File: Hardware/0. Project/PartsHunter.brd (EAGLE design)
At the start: 214 x 147 mm, 54 parts, among them IC1 PCF8574P, IC2 LM1117-3.3, Q1 16 MHz, U1 ATMEGA328P-AU

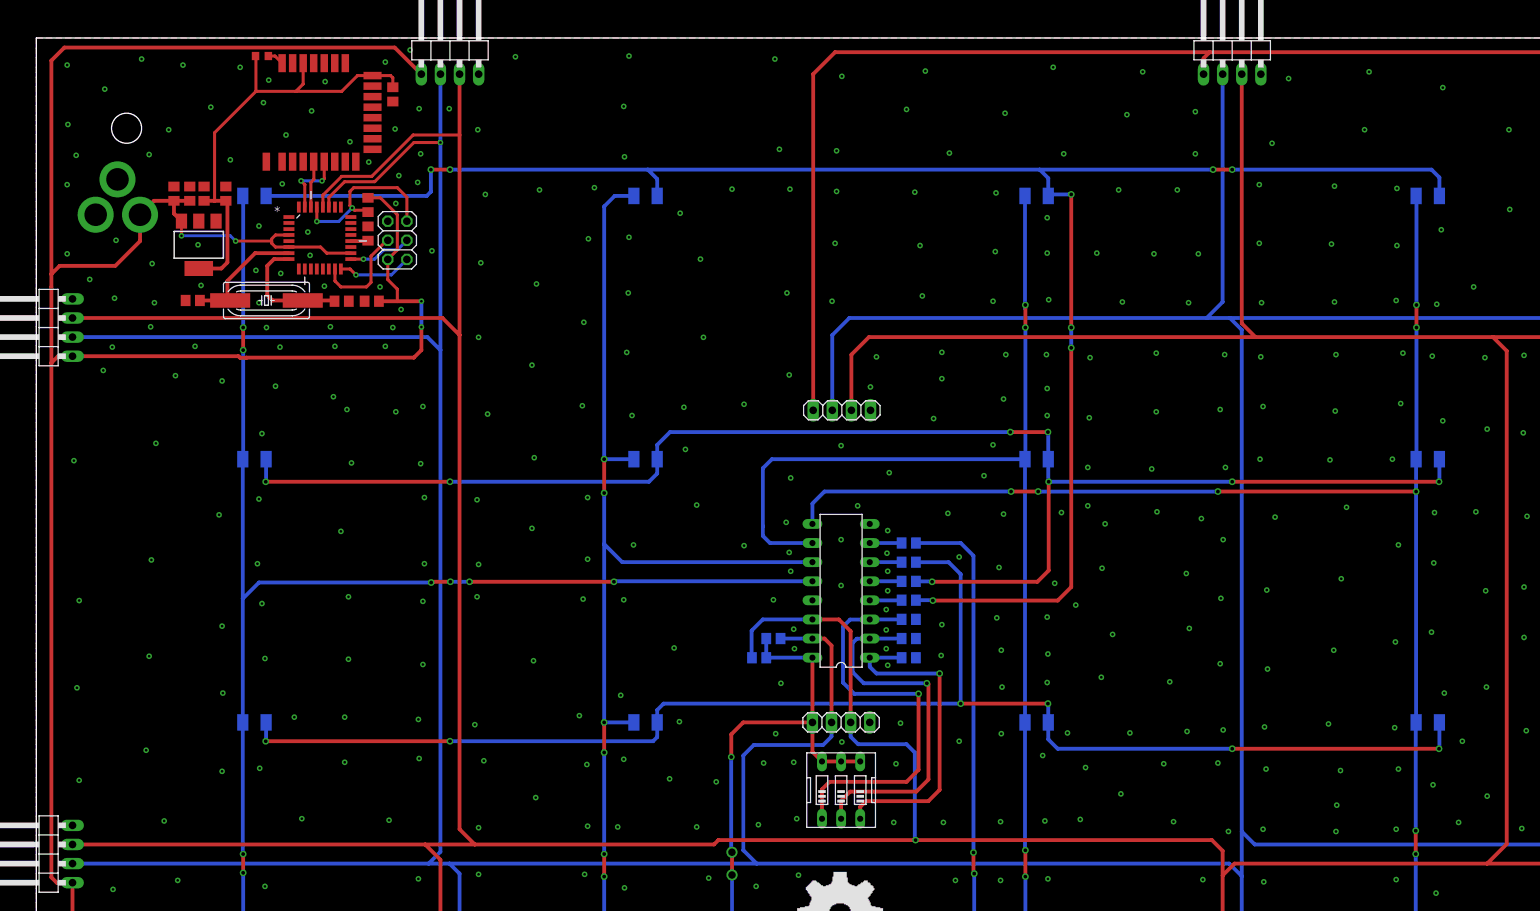
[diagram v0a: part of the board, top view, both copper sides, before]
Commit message: I2C pull-ups moved to master's circuit area
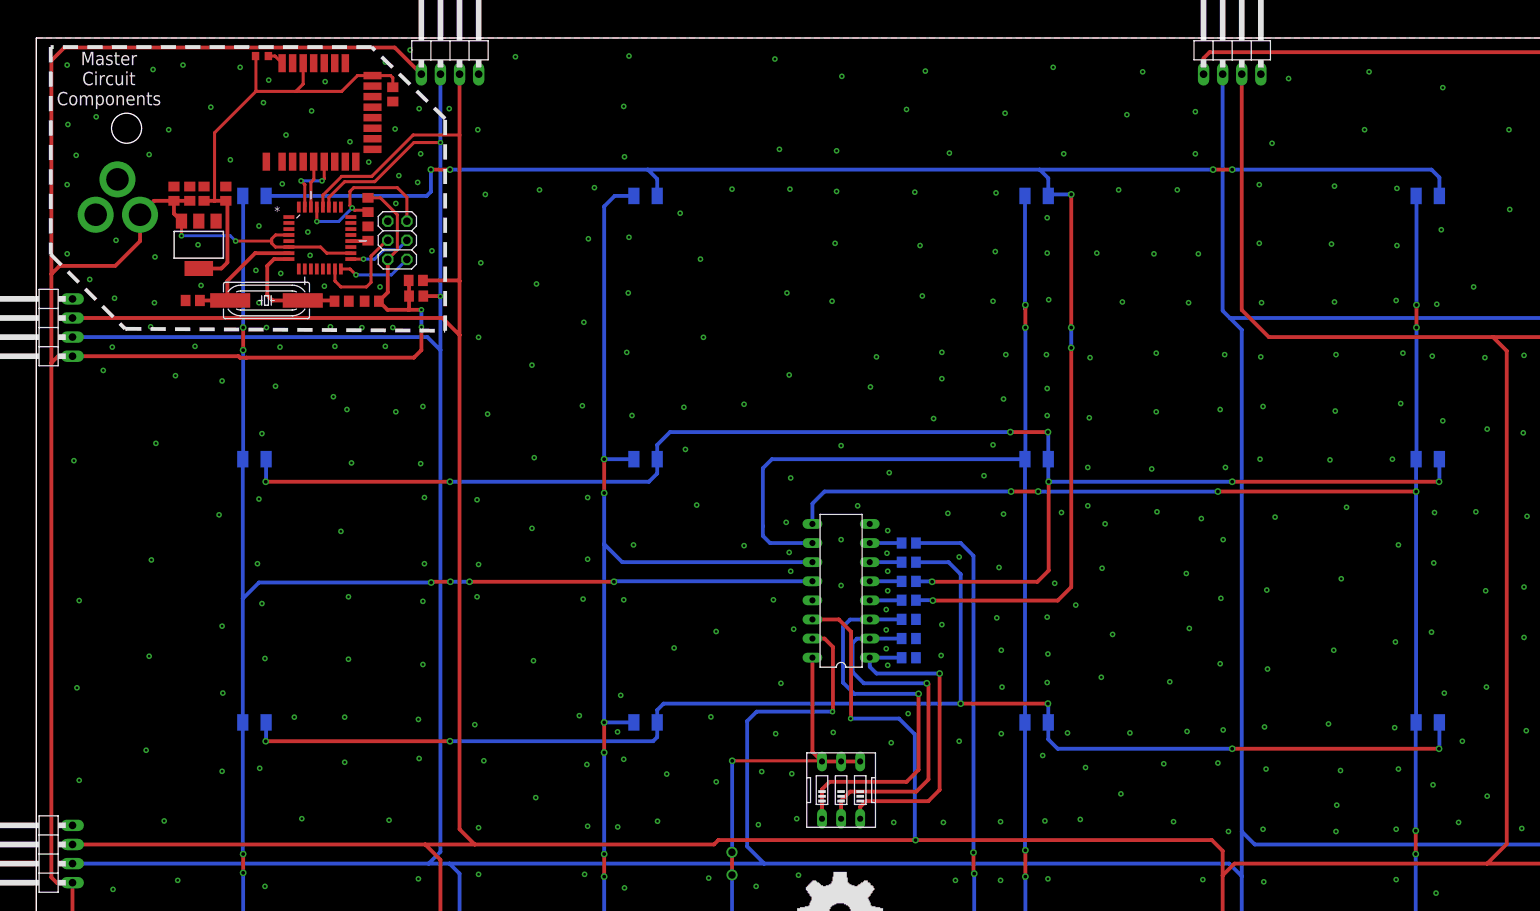
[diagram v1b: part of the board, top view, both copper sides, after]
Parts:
- removed JP10: (no value), pinhead:1X04
- removed JP12: ICSP, pinhead:2X03
- C3, C4: value 100 nF -> 22pF
- C6: value 10 uF -> 100 nF
- C7: value 22pF -> 10 uF
- C8: value 22pF -> 100 nF
- JP5: device pinhead:1X04 -> pinhead:1X04/90
- JP9: value (none) -> ICSP; device pinhead:1X04/90 -> pinhead:2X03
- R11: device rcl:R0603 -> rcl:R0805
- R6, R7: value 10k -> 72R
- R8: value 72R -> 10k; device rcl:R0805 -> rcl:R0603
- R9: value 72R -> 10k
- moved JP7 212.0 mm to (213.0, 38.5), turned to 270 degrees
- moved JP6 120.3 mm to (1.00, 38.5), turned to 90 degrees
- moved JP8 120.3 mm to (159.0, 146.0), turned to 0 degrees
- moved R11 117.5 mm to (116.0, 64.6), flipped to the bottom, turned to 180 degrees
- moved JP9 114.0 mm to (48.0, 120.1), turned to 90 degrees
- moved R8 109.2 mm to (30.0, 144.6), flipped to the top
- moved JP5 103.9 mm to (55.0, 146.0)
- moved R10 92.2 mm to (116.0, 67.2), flipped to the bottom, turned to 180 degrees
- moved R3 79.5 mm to (44.1, 124.8), flipped to the top, turned to 270 degrees
- moved R5 78.3 mm to (50.5, 112.7), flipped to the top, turned to 0 degrees
- moved R4 67.3 mm to (50.5, 114.8), flipped to the top, turned to 0 degrees
- moved C3 38.2 mm to (20.8, 112.1), turned to 0 degrees
- moved C5 25.8 mm to (47.4, 139.5), turned to 270 degrees
- moved C4 24.7 mm to (40.6, 112.0), turned to 180 degrees
- moved C8 24.7 mm to (20.4, 126.3), turned to 90 degrees
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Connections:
- net +5V: now also C8.1, C9.1, JP9.2, R5.1; no longer C4.1, C6.1, JP10.1, JP12.2, JP9.1, R10.1
- net 0V: now also C3.1, C4.1, C7.2, C8.2, JP9.6, R10.2, R11.2, R9.2; no longer C3.2, C4.2, C7.1, C8.1, JP10.4, JP12.6, JP9.4, R5.2, R6.2, R7.2
- net 3.3V: now also C6.1, C7.1, R8.1; no longer C3.1, C9.1, R11.1
- net BLE_WAKE: now also R8.2; no longer R11.2
- net ICSP_MISO: now also JP9.1; no longer JP12.1
- net ICSP_MOSI: now also JP9.4; no longer JP12.4
- net ICSP_RESET: now also JP9.5, R3.2; no longer JP12.5, R10.2
- net ICSP_SCK: now also JP9.3; no longer JP12.3
- net N$1: now also C3.2; no longer C7.2
- net N$2: now also C4.2; no longer C8.2
- net N$7: now also R6.1; no longer R8.1
- net N$8: now also R7.1; no longer R9.1
- net ROW_3: now also R6.2; no longer R8.2
- net ROW_4: now also R7.2; no longer R9.2
- net SCL: now also R4.2; no longer JP10.3, JP9.3, R3.2
- net SDA: now also R5.2; no longer JP10.2, JP9.2, R4.2
- net SLAVE_ADDR_A0: now also R11.1; no longer R7.1
- net SLAVE_ADDR_A1: now also R10.1; no longer R6.1
- net SLAVE_ADDR_A2: now also R9.1; no longer R5.1
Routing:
- net +5V: track 935.8 -> 828.6 mm
- net SCL: track 724.5 -> 654.0 mm, vias 1 -> 2
- net SDA: track 713.5 -> 648.0 mm, vias 1 -> 3
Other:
- board text added: "Master Circuit Components"

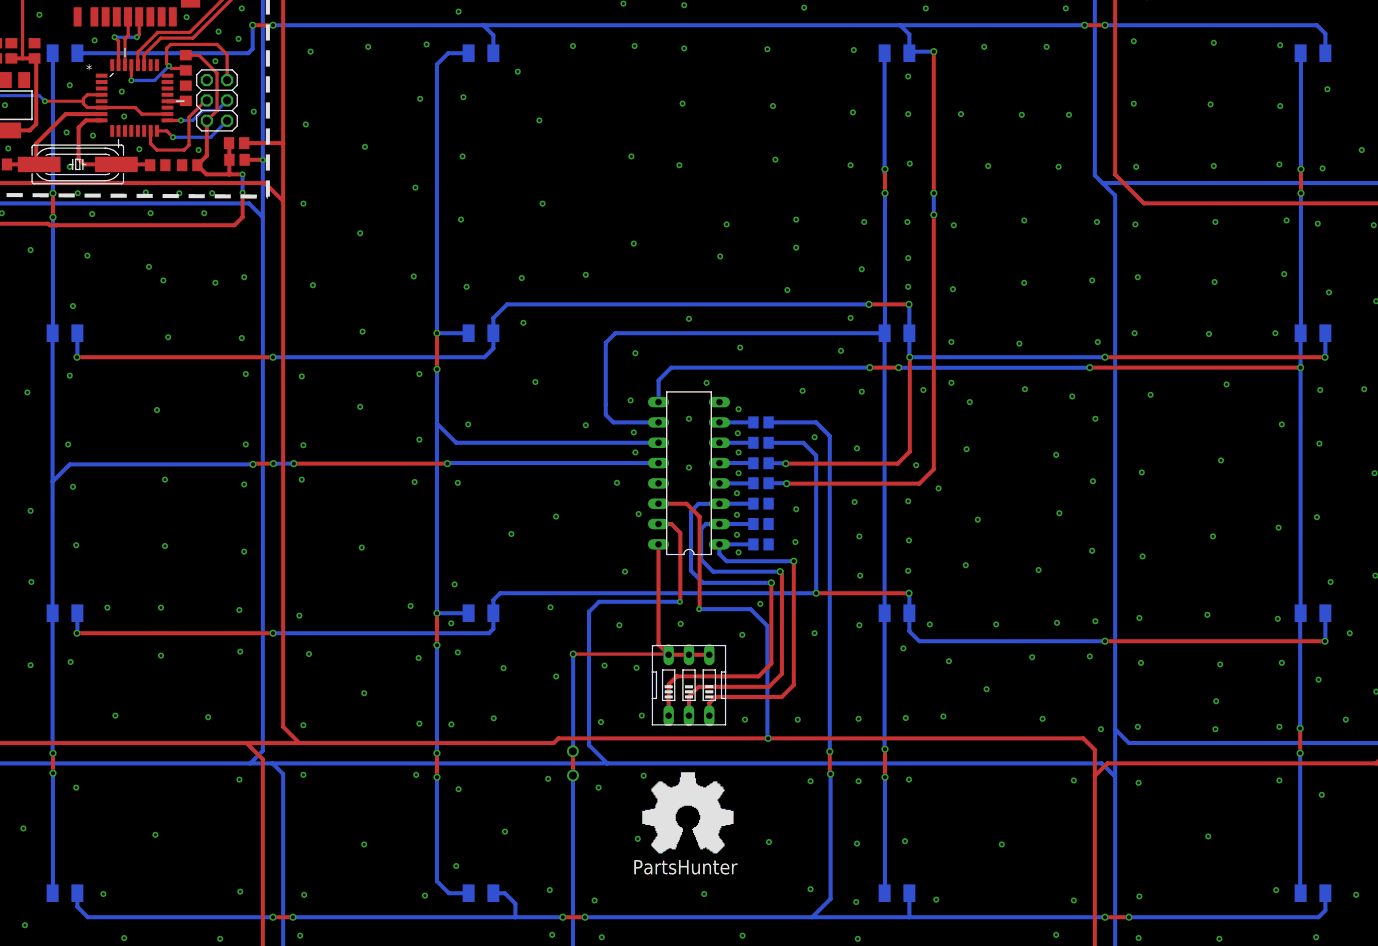
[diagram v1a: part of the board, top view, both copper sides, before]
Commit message: SMD and PTH led option added
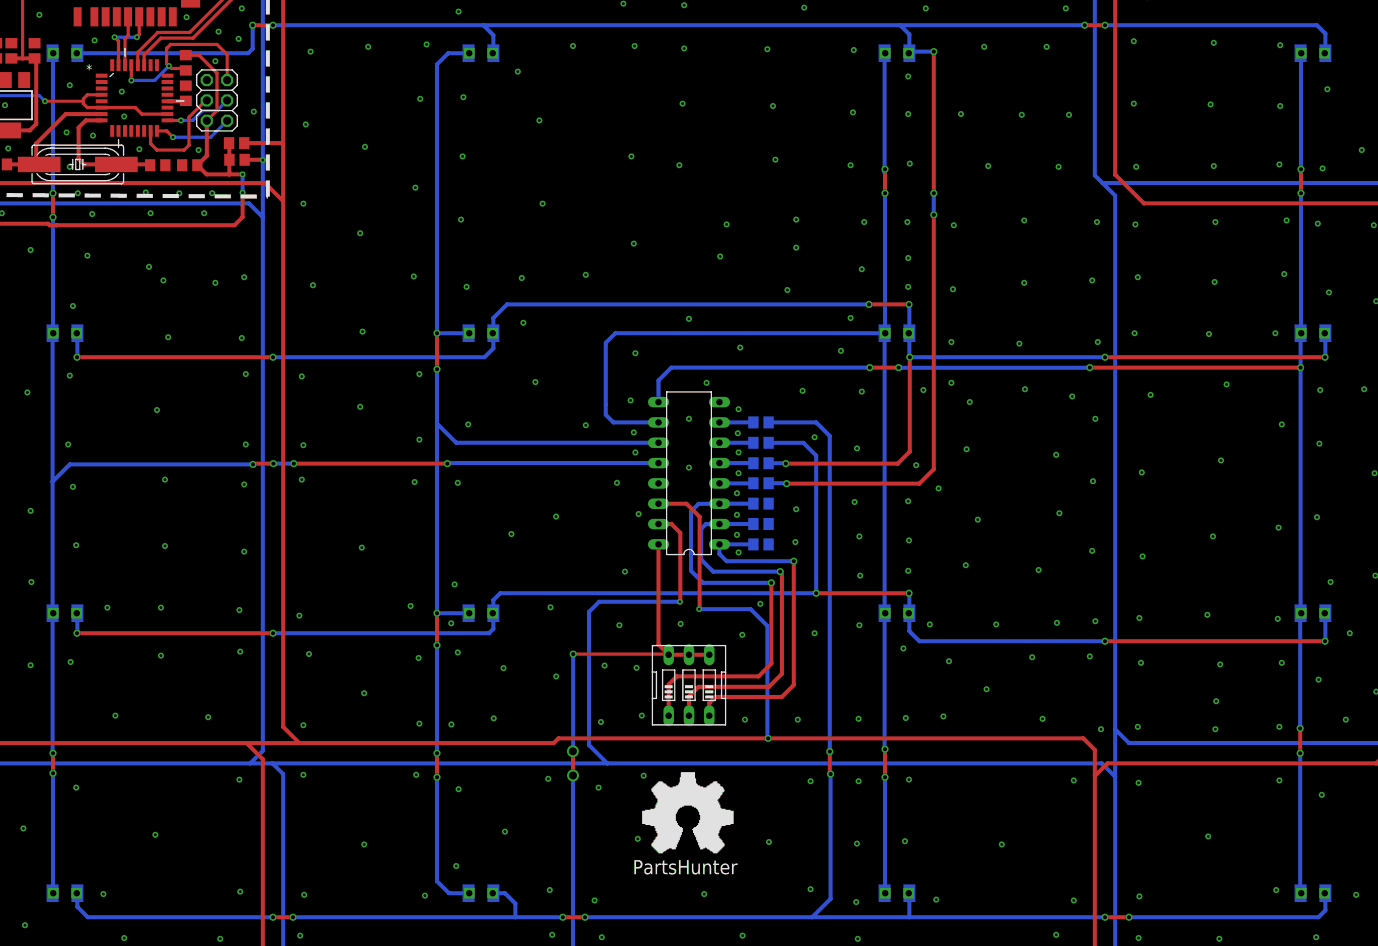
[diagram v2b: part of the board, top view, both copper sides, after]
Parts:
- LED1, LED10, LED11, LED12, LED13, LED14, LED15, LED16, LED2, LED3, LED4, LED5, LED6, LED7, LED8, LED9: device led:KA-3528ASYC -> led2:KA-3528ASYC
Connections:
- net COLUMN_1: now also LED1.P$2, LED13.P$2, LED5.P$2, LED9.P$2
- net COLUMN_2: now also LED10.P$2, LED14.P$2, LED2.P$2, LED6.P$2
- net COLUMN_3: now also LED11.P$2, LED15.P$2, LED3.P$2, LED7.P$2
- net COLUMN_4: now also LED12.P$2, LED16.P$2, LED4.P$2, LED8.P$2
- net N$5: now also LED1.P$1, LED2.P$1, LED3.P$1, LED4.P$1
- net N$6: now also LED5.P$1, LED6.P$1, LED7.P$1, LED8.P$1
- net N$7: now also LED10.P$1, LED11.P$1, LED12.P$1, LED9.P$1
- net N$8: now also LED13.P$1, LED14.P$1, LED15.P$1, LED16.P$1

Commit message: Working on 2.0 PCB (bug fix)
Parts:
- added Q2, Q3, Q4, Q5, Q6, Q7: AO3400A, AO3400A:SOT95P280X125-3N
- added R12, R13, R14, R15, R18, R19: 100R (5%), rcl:R0805
- added R16: 22k (5%), rcl:R0805
- added R17: 33k (5%), rcl:R0805
- CN1: value (none) -> 2.1MMJACKTHM
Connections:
- new net N$10: Q2.2, R2.2
- new net N$11: Q3.1, R14.2
- new net N$12: Q3.2, R6.2
- new net N$13: Q2.1, R13.2
- new net N$14: Q4.2, R7.2
- new net N$15: PCB1.6, R16.2, R17.2
- new net N$16: Q5.1, R18.2
- new net N$18: Q7.1, R19.2
- new net N$3: Q6.1, R12.2
- new net N$4: Q6.2, R1.2
- new net N$9: Q4.1, R15.2
- net +5V: now also Q2.3, Q3.3, Q4.3, Q6.3
- net 0V: now also Q5.2, Q7.2, R17.1
- net BLE_RX: now also R16.1; no longer PCB1.6
- net COLUMN_1: now also Q5.3
- net COLUMN_2: now also Q7.3
- net ROW_1: now also R12.1; no longer R1.2
- net ROW_2: now also R13.1; no longer R2.2
- net ROW_3: now also R14.1; no longer R6.2
- net ROW_4: now also R15.1; no longer R7.2
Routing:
- net ROW_4: track 4.24 -> 0.00 mm
- net BLE_RX: track 9.15 -> 6.90 mm
